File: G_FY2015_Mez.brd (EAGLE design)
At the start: 160 x 100 mm, 176 parts, among them IC100 FT232RL, J1 RPI2_GPIO_HOLES, J100 EPL.00.250.NTN, J101 EPL.00.250.NTN, J102 EPL.00.250.NTN, J103 EPL.00.250.NTN, J180 TOKUDEN_SP6, J2 SPACEWIRE_MDMMDM9, J300 SHV_PIGTAIL_LAND, J301 SHV_PIGTAIL_LAND, J600_12V IL-4P-S3EN2, J610 2.1MMJACKTHM, U1 AD8138, U10 LM60, U100 AD9215, U101 AD8138, U11 MCP4822-E/SN, U110 AD9215, U120 AD9215, U130 AD9215, U191 GPS_FGPMMOPA6H, U192 LED-5, U2 AD8138, U3 AD8138, U300 OPTON_1PA_12, U301 OPTON_1PA_12, U302 2SC1815, U303 2SJ313, U5 MCP3208-CI/SL, U500 LT6106, U510 LT6106, U6 MCP1525TSOT-23-3, U600 PHT12050WAH, U610 PHT12050WAH, U620 LTC1983ES6-3, U7 LM60, U8 LM60, U9 LM60

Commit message: first board layout completed
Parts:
- removed TP_PRE_IN1, TP_PRE_IN2, TP_PRE_IN3, TP_PRE_IN4, TP_PRE_OUT0, TP_PRE_OUT1, TP_PRE_OUT2, TP_PRE_OUT3: TPPAD1-17, Aardvark:P1-17
- removed U1, U2, U3: AD8138, Aardvark:SOIC-8(150MIL)(1.27MM)
- added P_IN0, P_IN1, P_IN2, P_IN3, P_OUT0, P_OUT1, P_OUT2, P_OUT3: TPPAD1-17, Aardvark:P1-17
- added U111, U121, U131: AD8138, Aardvark:SOIC-8(150MIL)(1.27MM)
- moved C103 308.4 mm to (127.0, 36.8)
- moved C102 304.0 mm to (133.3, 47.0)
- moved C101 303.9 mm to (137.2, 41.9), turned to 90 degrees
- moved TP102 297.3 mm to (147.3, 26.7), turned to 90 degrees
- moved C100 286.9 mm to (124.5, 41.9), turned to 90 degrees
- moved TP101 275.9 mm to (125.7, 21.6)
- moved R111 261.8 mm to (87.6, 71.1)
- moved TP104 260.3 mm to (102.9, 45.7), turned to 90 degrees
- moved R118 257.6 mm to (99.1, 83.8), turned to 270 degrees
- moved TP100 255.8 mm to (115.6, 33.0)
- moved TP113 254.6 mm to (78.7, 48.3)
- moved R116 250.0 mm to (87.6, 58.4), turned to 90 degrees
- moved R106 247.3 mm to (141.0, 26.7), turned to 270 degrees
- moved TP103 244.6 mm to (78.7, 26.7)
- moved R114 244.6 mm to (91.4, 58.4), turned to 90 degrees
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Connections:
- net +3V3: now also U111.3, U121.3, U131.3; no longer U1.3, U2.3, U3.3
- net -3V3: now also U111.6, U121.6, U131.6; no longer U1.6, U2.6, U3.6
- net ADC_CM: now also U111.2, U121.2, U131.2; no longer U1.2, U2.2, U3.2
- net N$37: now also U111.1; no longer U1.1
- net N$40: now also U111.8; no longer U1.8
- net N$41: now also U111.5; no longer U1.5
- net N$42: now also U111.4; no longer U1.4
- net N$43: now also U121.1; no longer U2.1
- net N$44: now also U121.8; no longer U2.8
- net N$45: now also U121.5; no longer U2.5
- net N$46: now also U121.4; no longer U2.4
- net N$47: now also U131.1; no longer U3.1
- net N$48: now also U131.8; no longer U3.8
- net N$49: now also U131.5; no longer U3.5
- net N$50: now also U131.4; no longer U3.4
- net N$58: now also P_IN0.TP; no longer TP_PRE_IN1.TP
- net N$70: now also P_IN1.TP; no longer TP_PRE_IN2.TP
- net N$75: now also P_IN2.TP; no longer TP_PRE_IN3.TP
- net N$80: now also P_IN3.TP; no longer TP_PRE_IN4.TP
- net PREAMP0_OUT: now also P_OUT0.TP; no longer TP_PRE_OUT0.TP
- net PREAMP1_OUT: now also P_OUT1.TP; no longer TP_PRE_OUT1.TP
- net PREAMP2_OUT: now also P_OUT2.TP; no longer TP_PRE_OUT2.TP
- net PREAMP3_OUT: now also P_OUT3.TP; no longer TP_PRE_OUT3.TP
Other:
- board text added: "Ch.0"
- board text added: "Ch.1"
- board text added: "Ch.2"

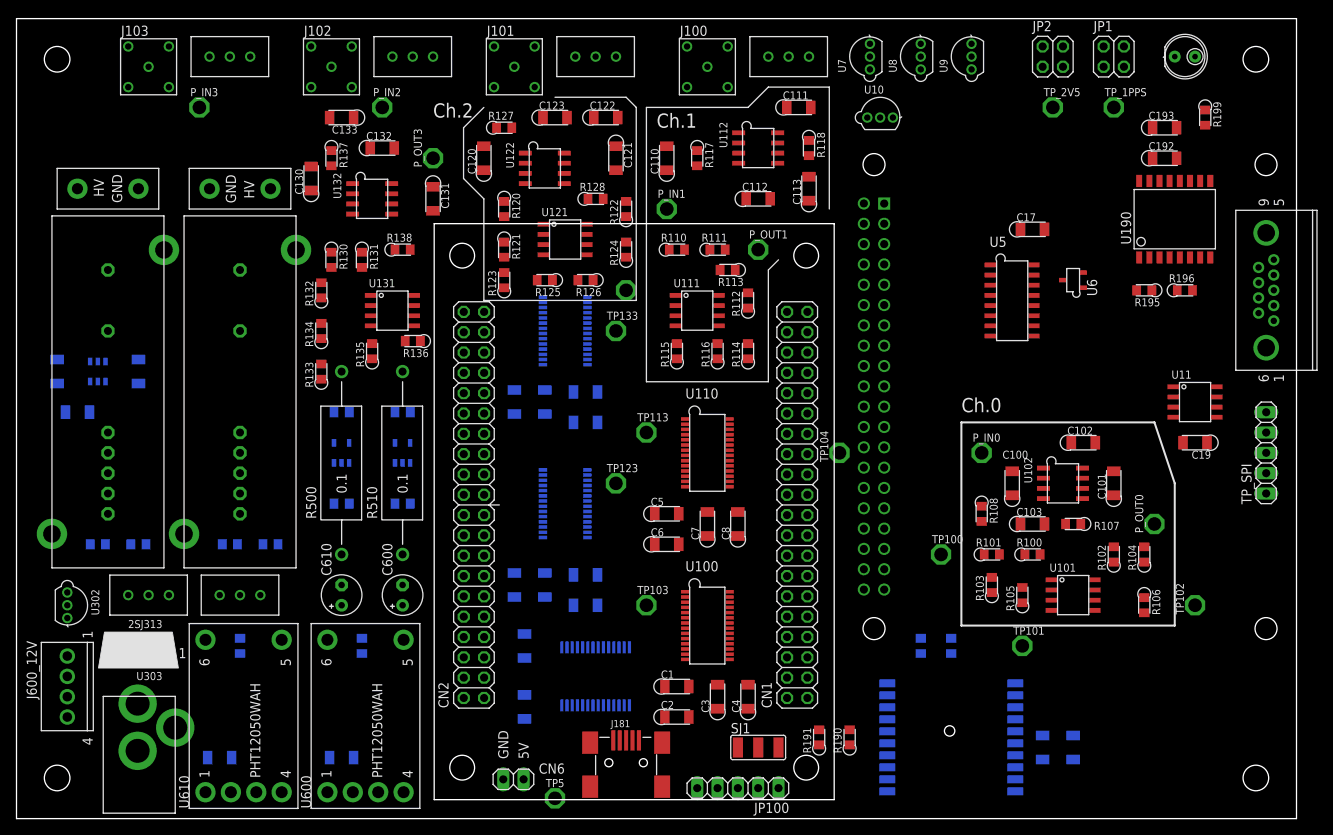
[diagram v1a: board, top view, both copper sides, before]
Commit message: board layout completed, 100% routerd, logo inserted
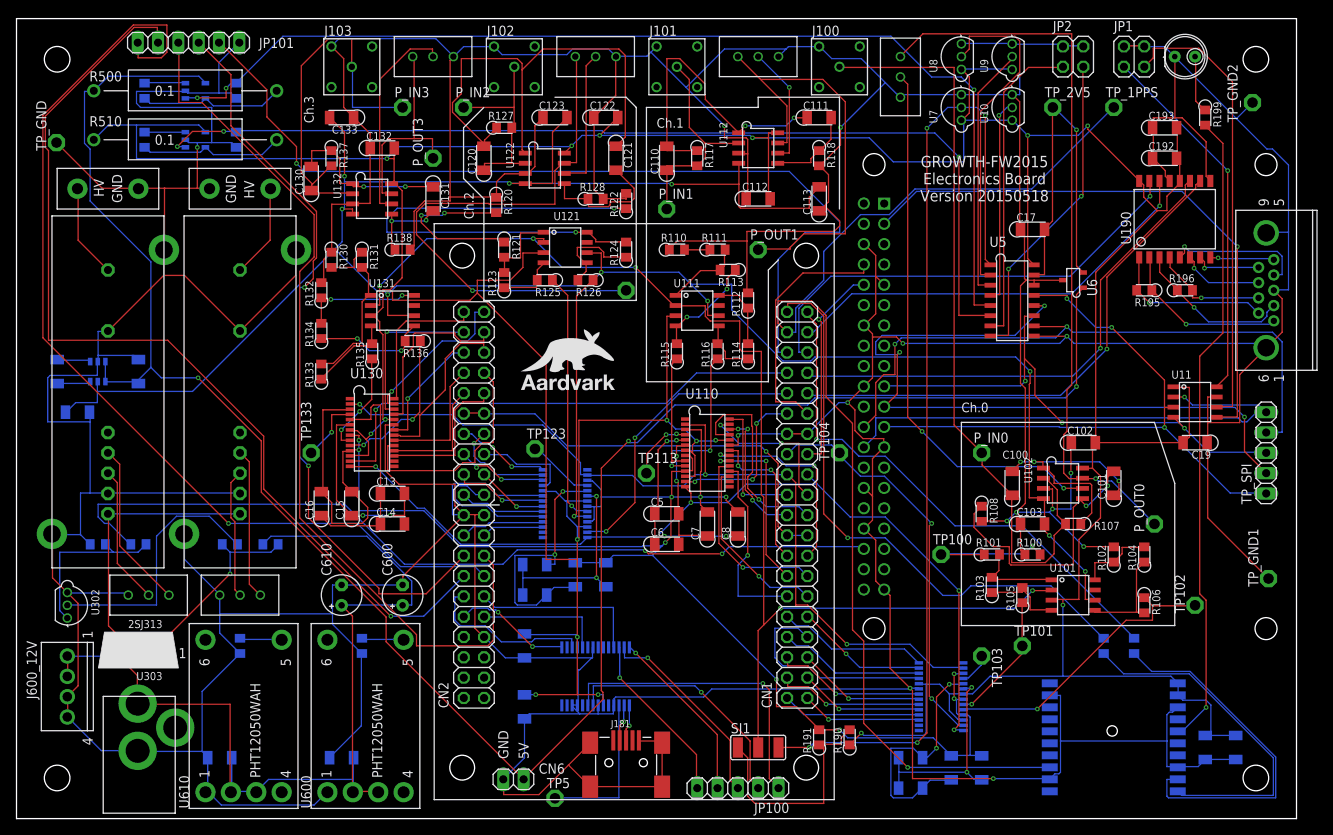
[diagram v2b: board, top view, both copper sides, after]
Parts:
- added JP101: (no value), pinhead:1X06
- added TP_GND, TP_GND1, TP_GND2: TPPAD1-13, Aardvark:P1-13
- added U$27: (no value), Aardvark:AARDVARK_LOGO
- J181: value (none) -> USB Mini-B Connector
- P_IN0, P_IN1, P_IN2, P_IN3, P_OUT0, P_OUT1, P_OUT2, P_OUT3, TP100, TP101, TP102, TP103, TP104, TP113, TP123, TP133, TP5, TP_1PPS, TP_2V5: value TPPAD1-17 -> TPPAD1-13; device Aardvark:P1-17 -> Aardvark:P1-13
- R190, R191, VR100, VR110, VR120, VR130: value (none) -> 1k
- R195, R196: value (none) -> 100
- U102, U112, U122, U132: value (none) -> LM6142
- U190: value (none) -> SN65LVDS049
- VR300, VR301: value (none) -> 5k
- moved R501 57.2 mm to (16.0, 91.0), turned to 90 degrees
- moved R511 55.8 mm to (16.0, 84.9), turned to 90 degrees
- moved R500 50.5 mm to (21.1, 91.0), turned to 0 degrees
- moved U500 48.8 mm to (22.4, 91.0), turned to 90 degrees
- moved R510 48.7 mm to (21.1, 84.9), turned to 0 degrees
- moved U510 46.9 mm to (22.4, 84.9), turned to 90 degrees
- moved TP103 42.4 mm to (120.7, 20.3), turned to 270 degrees
- moved R502 42.3 mm to (27.4, 91.0), turned to 90 degrees
- moved TP133 41.0 mm to (36.8, 45.7), turned to 90 degrees
- moved R512 39.9 mm to (27.4, 84.9), turned to 90 degrees
- moved C3 34.2 mm to (120.7, 6.35), flipped to the bottom
- moved C1 30.5 mm to (111.8, 7.62), flipped to the bottom
- moved C2 30.5 mm to (111.8, 3.81), flipped to the bottom
- moved U100 30.5 mm to (115.6, 15.2), flipped to the bottom
- moved C15 27.3 mm to (41.9, 39.4), flipped to the top
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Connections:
- removed net AAA: J180.36
- removed net BBB: J180.51
- removed net N$34: J181.5, J181.P$1, J181.P$2, J181.P$3
- removed net N$93: J2.THREAD_1
- removed net NNN: J180.55
- new net FPGA_GPIO0: J180.36, JP101.5
- new net FT232_/CTS_FPGA_/RTS: IC100.11, J180.51
- new net FT232_/RTS_FPGA_/CTS: IC100.3, J180.52
- new net TRIG_OUT0: J180.53, JP101.1
- new net TRIG_OUT1: J180.54, JP101.2
- new net TRIG_OUT2: J180.55, JP101.3
- new net TRIG_OUT3: J180.56, JP101.4
- net ADC2_D7: now also J180.66
- net GND: now also J181.5, J181.P$1, J181.P$2, J181.P$3, J2.THREAD_1, JP101.6, TP_GND.TP, TP_GND1.TP, TP_GND2.TP
- net N$24: now also IC100.10; no longer J180.53
- net N$26: now also IC100.9; no longer J180.56
- net N$27: now also IC100.2; no longer J180.54
- net N$28: now also IC100.6; no longer J180.52
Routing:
- net GND: track 0.00 -> 873.4 mm, vias 0 -> 7
- net +3V3: track 0.00 -> 602.5 mm, vias 0 -> 17
- net AGND: track 0.00 -> 401.5 mm, vias 0 -> 7
- net -3V3: track 0.00 -> 293.1 mm, vias 0 -> 10
- net +5V: track 0.00 -> 256.9 mm, vias 0 -> 3
- net GNDA: track 0.00 -> 218.9 mm, vias 0 -> 10
- net ADC_CM: track 0.00 -> 151.9 mm, vias 0 -> 5
- net GPS_1PPS: track 0.00 -> 146.0 mm, vias 0 -> 1
- net SLOWADC_4: track 0.00 -> 134.3 mm, vias 0 -> 3
- net SLOWADC_5: track 0.00 -> 124.9 mm, vias 0 -> 3
- net TRIG_OUT0: track 0.00 -> 124.7 mm, vias 0 -> 1
- net +12V: track 0.00 -> 123.8 mm
- net SLOWADC_0: track 0.00 -> 122.7 mm, vias 0 -> 4
- net TRIG_OUT1: track 0.00 -> 120.9 mm, vias 0 -> 1
- net FPGA_GPIO0: track 0.00 -> 113.2 mm, vias 0 -> 1
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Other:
- board text added: "Ch.3"
- board text added: "GROWTH-FW2015 Electronics Board Version 20150518"

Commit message: GNDA and AGND removed (just use GND)
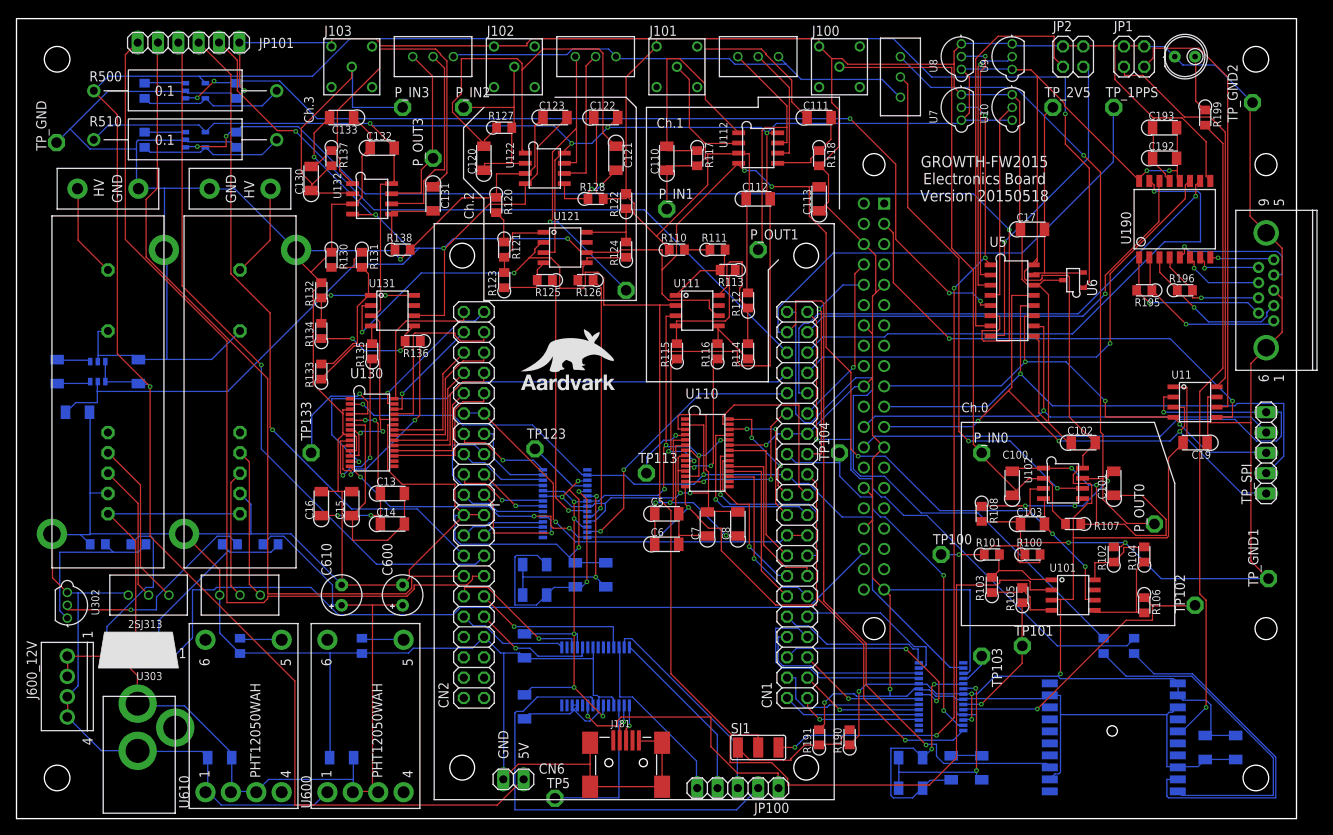
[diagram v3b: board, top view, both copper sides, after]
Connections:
- removed net GNDA: C11.2, C12.2, C15.2, C16.2, C3.2, C4.2, C7.2, C8.2, R191.2, U100.11, U100.3, U100.8, U110.11, U110.3, U110.8, U120.11, U120.3, U120.8, U130.11, U130.3, U130.8
- net AGND: no longer C102.1, C103.1, C112.1, C113.1, C122.1, C123.1, C132.1, C133.1, C17.1, J100.S1, J101.S1, J102.S1, J103.S1, JP2.2, JP2.4, R100.1, R102.2, R108.2, R110.1, R112.2, R118.2, R120.1, R122.2, R128.2, R130.1, R132.2, R138.2, U10.3, U102.3, U112.3, U122.3, U132.3, U5.14, U6.3, U7.3, U8.3, U9.3
- net GND: now also C102.1, C103.1, C11.2, C112.1, C113.1, C12.2, C122.1, C123.1, C132.1, C133.1, C15.2, C16.2, C17.1, C3.2, C4.2, C7.2, C8.2, J100.S1, J101.S1, J102.S1, J103.S1, JP2.2, JP2.4, R100.1, R102.2, R108.2, R110.1, R112.2, R118.2, R120.1, R122.2, R128.2, R130.1, R132.2, R138.2, R191.2, U10.3, U100.11, U100.3, U100.8, U102.3, U110.11, U110.3, U110.8, U112.3, U120.11, U120.3, U120.8, U122.3, U130.11, U130.3, U130.8, U132.3, U5.14, U6.3, U7.3, U8.3, U9.3
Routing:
- net GND: track 873.4 -> 1355.2 mm, vias 7 -> 12
- net AGND: track 401.5 -> 60.1 mm, vias 7 -> 0
- net GNDA: track 218.9 -> 0.00 mm, vias 10 -> 0
- net N$44: track 62.8 -> 9.13 mm, vias 2 -> 0
- net ADC_CM: track 151.9 -> 191.4 mm, vias 5 -> 2
- net +5V: track 256.9 -> 293.2 mm, vias 3 -> 2
- net PREAMP2_OUT: track 70.4 -> 41.0 mm
- net N$78: track 21.0 -> 49.7 mm, vias 2 -> 0
- net +3V3: track 602.5 -> 578.3 mm, vias 17 -> 21
- net N$22: track 31.2 -> 55.2 mm, vias 1 -> 0
- net FPGA_GPIO0: track 113.2 -> 89.3 mm
- net TRIG_OUT2: track 111.9 -> 89.4 mm, vias 0 -> 1
- net HV_PWR_ENADIS: track 107.4 -> 129.7 mm, vias 2 -> 0
- net PREAMP1_OUT: track 54.5 -> 32.8 mm
- net TRIG_OUT1: track 120.9 -> 102.2 mm, vias 1 -> 0
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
